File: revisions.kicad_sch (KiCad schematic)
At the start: 0 parts

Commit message: Continued additional minor cleanups
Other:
- note added: "* Fix connections for 3.5mm jacks (tip & sleeve were reversed) * Revise MIDI In circuits with smaller opto-isolator ... * Miscellaneous cleanups"
- note removed: "* Fix connections for 3.5mm jacks (tip & sleeve were reversed)"
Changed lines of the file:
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@@
 	(title_block
 		(title "Revision History")
-		(date "2024-11-05")
+		(date "2024-11-06")
 		(rev "2")
 		(company "Douglas P. Fields, Jr.")
@@
 		)
 	)
-	(text "* Fix connections for 3.5mm jacks (tip & sleeve were reversed)"
+	(text "* Fix connections for 3.5mm jacks (tip & sleeve were reversed)\n* Revise MIDI In circuits with smaller opto-isolator\n...\n* Miscellaneous cleanups"
 		(exclude_from_sim no)
 		(at 25.4 42.418 0)
@@
 				(thickness 0.1588)
 			)
-			(justify left)
+			(justify left top)
 		)
 	)

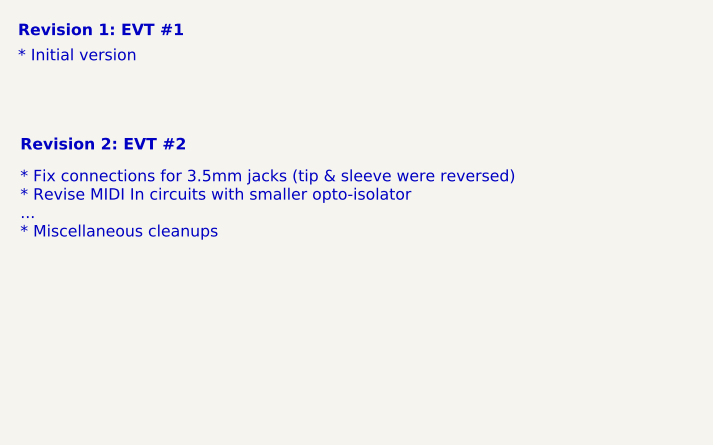
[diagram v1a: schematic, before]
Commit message: Add 5V test pins
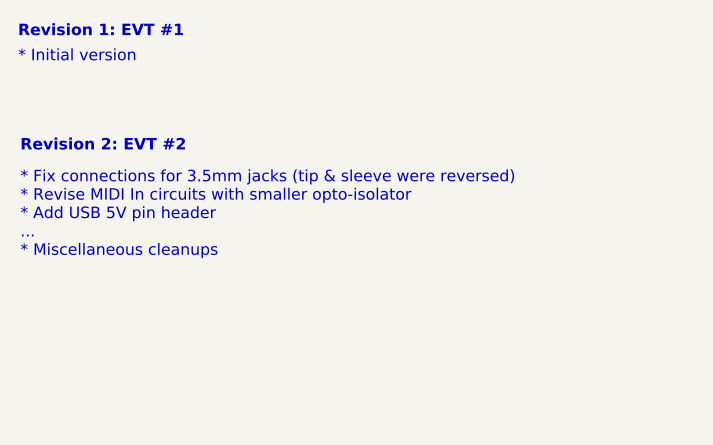
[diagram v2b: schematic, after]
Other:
- note added: "* Fix connections for 3.5mm jacks (tip & sleeve were reversed) * Revise MIDI In circuits with smaller opto-isolator * Add USB 5V pin header ... * Miscellaneous cleanups"
- note removed: "* Fix connections for 3.5mm jacks (tip & sleeve were reversed) * Revise MIDI In circuits with smaller opto-isolator ... * Miscellaneous cleanups"
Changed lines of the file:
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@@
 	(title_block
 		(title "Revision History")
-		(date "2024-11-06")
+		(date "2024-11-10")
 		(rev "2")
 		(company "Douglas P. Fields, Jr.")
@@
 		)
 	)
-	(text "* Fix connections for 3.5mm jacks (tip & sleeve were reversed)\n* Revise MIDI In circuits with smaller opto-isolator\n...\n* Miscellaneous cleanups"
+	(text "* Fix connections for 3.5mm jacks (tip & sleeve were reversed)\n* Revise MIDI In circuits with smaller opto-isolator\n* Add USB 5V pin header\n...\n* Miscellaneous cleanups"
 		(exclude_from_sim no)
 		(at 25.4 42.418 0)

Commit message: More revisions for EVT2: 1. Move GAIN0/1 to MCU pins. 2. Revise SPI header with additional screen GPIO. 3. Revise GPIO header due to 1 and 2.
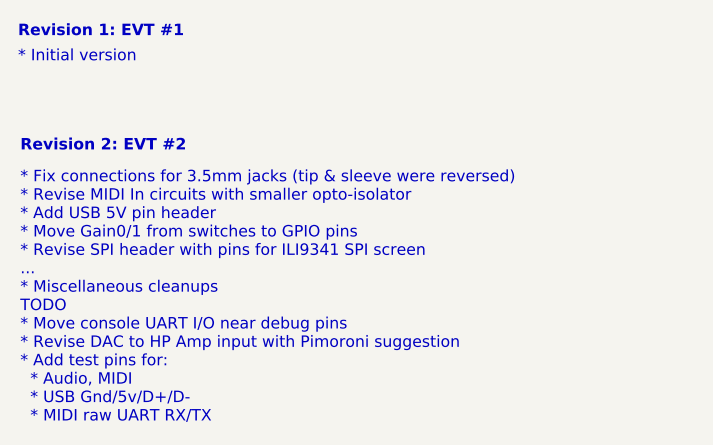
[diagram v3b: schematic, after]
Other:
- note added: "* Fix connections for 3.5mm jacks (tip & sleeve were reversed) * Revise MIDI In circuits with smaller opto-isolator * Add USB 5V pin header * Move Gain0/1 from switches to GPIO pins * Revise SPI header with pins for ILI9341 SPI screen ... * Miscellaneous cleanups TODO * Move console UART I/O near debug pins * Revise DAC to HP Amp input with Pimoroni suggestion * Add test pins for: * Audio, MIDI *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"
- note removed: "* Fix connections for 3.5mm jacks (tip & sleeve were reversed) * Revise MIDI In circuits with smaller opto-isolator * Add USB 5V pin header ... * Miscellaneous cleanups"
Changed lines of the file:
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@@
 		)
 	)
-	(text "* Fix connections for 3.5mm jacks (tip & sleeve were reversed)\n* Revise MIDI In circuits with smaller opto-isolator\n* Add USB 5V pin header\n...\n* Miscellaneous cleanups"
+	(text "* Fix connections for 3.5mm jacks (tip & sleeve were reversed)\n* Revise MIDI In circuits with smaller opto-isolator\n* Add USB 5V pin header\n* Move Gain0/1 from switches to GPIO pins\n* Revise SPI header with pins for ILI9341 SPI screen\n...\n* Miscellaneous cleanups\nTODO\n* Move console UART I/O near debug pins\n* Revise DAC to HP Amp input with Pimoroni suggestion\n* Add test pins for:\n  * Audio, MIDI\n  * USB Gnd/5v/D+/D-\n  * MIDI raw UART RX/TX\n"
 		(exclude_from_sim no)
 		(at 25.4 42.418 0)
